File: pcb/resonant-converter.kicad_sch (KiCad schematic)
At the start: 60 parts, among them J1 Banana_Jack_Keystone_575-8, J2 Banana_Jack_Keystone_575-8, J3 Banana_Jack_Keystone_575-8, J4 Banana_Jack_Keystone_575-8, Q1 MDU04N010VRH, Q2 MDU04N010VRH, Q3 HSU30N20, Q4 HSU30N20, T1 B66206W1110T001, U1 UCC256610DDBR, U2 TEA2096T/1J, U4 PC817X2CSP9F, U5 TL431AIDBVR

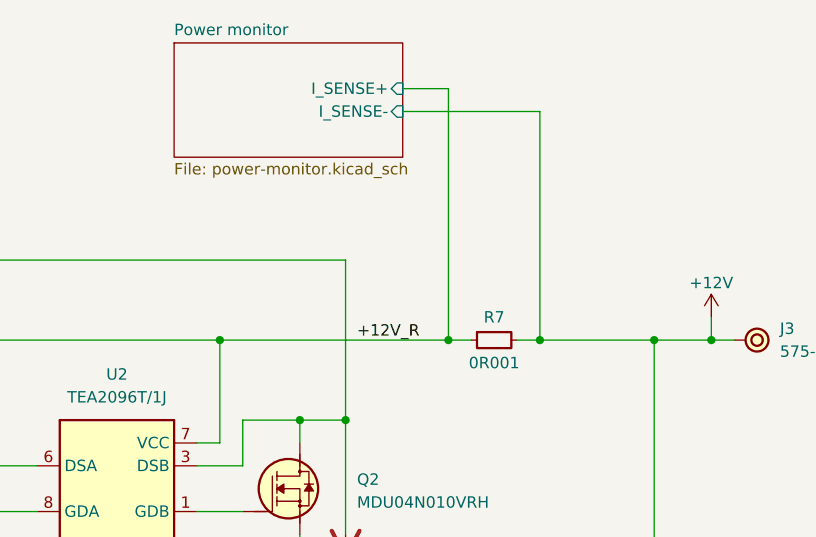
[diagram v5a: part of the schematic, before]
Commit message: [#4] Sch: Add I2C pullups, write down INA219's address, add hierarchical label for power monitor's GND
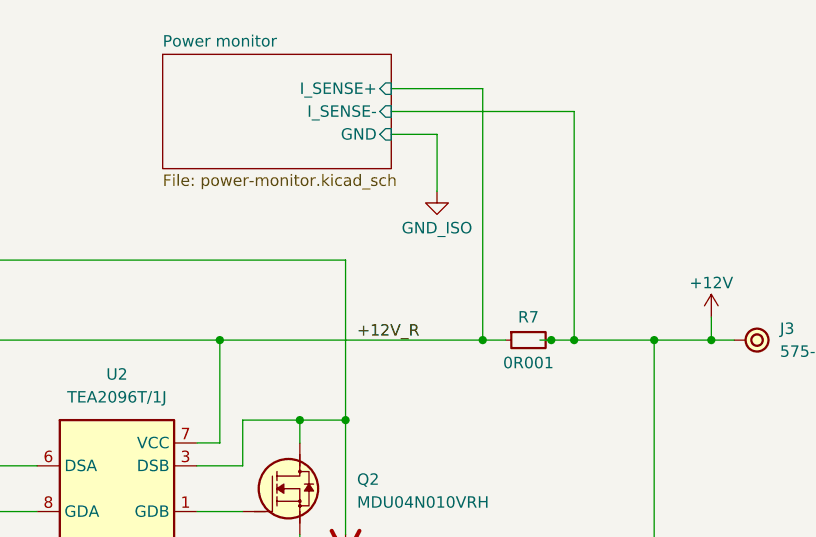
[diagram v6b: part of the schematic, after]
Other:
- sheet Power monitor ports: added GND; removed none
- moved on the sheet: R7
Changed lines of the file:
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@@
 	)
 	(junction
-		(at 361.95 107.95)
-		(diameter 0)
-		(color 0 0 0 0)
-	)
-	(junction
 		(at 369.57 147.32)
 		(diameter 0)
@@
 	)
 	(junction
-		(at 372.11 107.95)
-		(diameter 0)
-		(color 0 0 0 0)
-	)
-	(junction
 		(at 142.24 116.84)
 		(diameter 0)
@@
 	)
 	(junction
+		(at 373.38 107.95)
+		(diameter 0)
+		(color 0 0 0 0)
+	)
+	(junction
 		(at 345.44 132.08)
 		(diameter 0)
@@
 	)
 	(junction
+		(at 375.92 107.95)
+		(diameter 0)
+		(color 0 0 0 0)
+	)
+	(junction
 		(at 33.02 152.4)
 		(diameter 0)
@@
 	)
 	(junction
+		(at 365.76 107.95)
+		(diameter 0)
+		(color 0 0 0 0)
+	)
+	(junction
 		(at 306.07 147.32)
 		(diameter 0)
@@
 	(wire
 		(pts
+			(xy 365.76 107.95) (xy 368.3 107.95)
+		)
+		(stroke
+			(width 0)
+			(type default)
+		)
+	)
+	(wire
+		(pts
 			(xy 369.57 161.29) (xy 369.57 147.32)
 		)
@@
 	(wire
 		(pts
-			(xy 361.95 80.01) (xy 361.95 107.95)
+			(xy 365.76 80.01) (xy 365.76 107.95)
 		)
 		(stroke
@@
 	(wire
 		(pts
+			(xy 360.68 85.09) (xy 355.6 85.09)
+		)
+		(stroke
+			(width 0)
+			(type default)
+		)
+	)
+	(wire
+		(pts
 			(xy 304.8 116.84) (xy 311.15 116.84)
 		)
@@
 	(wire
 		(pts
-			(xy 361.95 107.95) (xy 364.49 107.95)
-		)
-		(stroke
-			(width 0)
-			(type default)
-		)
-	)
-	(wire
-		(pts
 			(xy 384.81 147.32) (xy 375.92 147.32)
 		)
@@
 	(wire
 		(pts
+			(xy 375.92 107.95) (xy 373.38 107.95)
+		)
+		(stroke
+			(width 0)
+			(type default)
+		)
+	)
+	(wire
+		(pts
 			(xy 304.8 116.84) (xy 304.8 119.38)
 		)
@@
 	(wire
 		(pts
+			(xy 373.38 107.95) (xy 372.11 107.95)
+		)
+		(stroke
+			(width 0)
+			(type default)
+		)
+	)
+	(wire
+		(pts
 			(xy 356.87 147.32) (xy 363.22 147.32)
 		)
@@
 	(wire
 		(pts
+			(xy 375.92 107.95) (xy 384.81 107.95)
+		)
+		(stroke
+			(width 0)
+			(type default)
+		)
+	)
+	(wire
+		(pts
 			(xy 39.37 147.32) (xy 39.37 152.4)
 		)
@@
 	(wire
 		(pts
-			(xy 372.11 107.95) (xy 384.81 107.95)
-		)
-		(stroke
-			(width 0)
-			(type default)
-		)
-	)
-	(wire
-		(pts
 			(xy 322.58 147.32) (xy 328.93 147.32)
 		)
@@
 	(wire
 		(pts
-			(xy 336.55 107.95) (xy 361.95 107.95)
+			(xy 336.55 107.95) (xy 365.76 107.95)
 		)
 		(stroke
@@
 	(wire
 		(pts
-			(xy 372.11 107.95) (xy 372.11 82.55)
+			(xy 375.92 107.95) (xy 375.92 82.55)
 		)
 		(stroke
@@
 	(wire
 		(pts
-			(xy 356.87 82.55) (xy 372.11 82.55)
+			(xy 355.6 82.55) (xy 375.92 82.55)
 		)
 		(stroke
@@
 	(wire
 		(pts
+			(xy 360.68 91.44) (xy 360.68 85.09)
+		)
+		(stroke
+			(width 0)
+			(type default)
+		)
+	)
+	(wire
+		(pts
 			(xy 294.64 147.32) (xy 302.26 147.32)
 		)
@@
 	(wire
 		(pts
-			(xy 356.87 80.01) (xy 361.95 80.01)
+			(xy 355.6 80.01) (xy 365.76 80.01)
 		)
 		(stroke
@@
 	(wire
 		(pts
-			(xy 369.57 107.95) (xy 372.11 107.95)
-		)
-		(stroke
-			(width 0)
-			(type default)
-		)
-	)
-	(wire
-		(pts
 			(xy 102.87 129.54) (xy 102.87 125.73)
 		)
@@
 	(symbol
 		(lib_id "DW-resistors:R-0R001-1206")
-		(at 364.49 107.95 0)
+		(at 368.3 107.95 0)
 		(unit 1)
 		(exclude_from_sim no)
@@
 		(dnp no)
 		(property "Reference" "R7"
-			(at 367.03 105.41 0)
+			(at 370.84 105.41 0)
 			(effects
 				(font
@@
 		)
 		(property "Value" "R-0R001-1206"
-			(at 377.19 110.49 0)
+			(at 381 110.49 0)
 			(effects
 				(font
@@
 		)
 		(property "Footprint" "DW-footprints:R_1206_3216Metric"
-			(at 377.19 113.03 0)
+			(at 381 113.03 0)
 			(effects
 				(font
@@
 		)
 		(property "Datasheet" "https://www.lcsc.com/datasheet/C7419993.pdf"
-			(at 377.19 115.57 0)
+			(at 381 115.57 0)
 			(effects
 				(font
@@
 		)
 		(property "Description" "1W 1mΩ ±50ppm/℃ Current Sense Resistor ±5% 1206 Current Sense Resistors RoHS"
-			(at 377.19 118.11 0)
+			(at 381 118.11 0)
 			(effects
 				(font
@@
 		)
 		(property "Manufacturer" "FOJAN"
-			(at 377.19 120.65 0)
+			(at 381 120.65 0)
 			(effects
 				(font
@@
 		)
 		(property "MPN" "FRM121WJR001TM"
-			(at 377.19 123.19 0)
+			(at 381 123.19 0)
 			(effects
 				(font
@@
 		)
 		(property "LCSC" "C7419993"
-			(at 377.19 125.73 0)
+			(at 381 125.73 0)
 			(effects
 				(font
@@
 		)
 		(property "Val" "0R001"
-			(at 367.03 110.49 0)
+			(at 370.84 110.49 0)
 			(effects
 				(font
@@
 		)
 		(property "Tolerance" "5%"
-			(at 377.19 130.81 0)
+			(at 381 130.81 0)
 			(effects
 				(font
@@
 	)
 	(symbol
+		(lib_id "DW-power-symbols:GND")
+		(at 360.68 91.44 0)
+		(unit 1)
+		(exclude_from_sim no)
+		(in_bom yes)
+		(on_board yes)
+		(dnp no)
+		(property "Reference" "#PWR019"
+			(at 360.68 97.79 0)
+			(effects
+				(font
+					(size 1.27 1.27)
+				)
+				(hide yes)
+			)
+		)
+		(property "Value" "GND_ISO"
+			(at 360.68 95.504 0)
+			(effects
+				(font
+					(size 1.27 1.27)
+				)
+			)
+		)
+		(property "Footprint" ""
+			(at 360.68 91.44 0)
+			(effects
+				(font
+					(size 1.27 1.27)
+				)
+				(hide yes)
+			)
+		)
+		(property "Datasheet" ""
+			(at 360.68 91.44 0)
+			(effects
+				(font
+					(size 1.27 1.27)
+				)
+				(hide yes)
+			)
+		)
+		(property "Description" "Power symbol creates a global label with name \"GND\" , ground"
+			(at 360.68 91.44 0)
+			(effects
+				(font
+					(size 1.27 1.27)
+				)
+				(hide yes)
+			)
+		)
+		(pin "1"
+		)
+		(instances
+			(project "resonant-converter"
+				(path "/da6185c3-cd85-4a88-bee6-2ff386eae772"
+					(reference "#PWR019")
+					(unit 1)
+				)
+			)
+		)
+	)
+	(symbol
 		(lib_id "DW-capacitors:C-10u-0603")
 		(at 322.58 166.37 90)
@@
 	)
 	(sheet
-		(at 331.47 74.93)
+		(at 330.2 76.2)
 		(size 25.4 12.7)
 		(exclude_from_sim no)
@@
 		)
 		(property "Sheetname" "Power monitor"
-			(at 331.47 74.2184 0)
+			(at 330.2 75.4884 0)
 			(effects
 				(font
@@
 		)
 		(property "Sheetfile" "power-monitor.kicad_sch"
-			(at 331.47 88.2146 0)
+			(at 330.2 89.4846 0)
 			(effects
 				(font
@@
 		)
 		(pin "I_SENSE-" input
-			(at 356.87 82.55 0)
+			(at 355.6 82.55 0)
 			(effects
 				(font
@@
 		)
 		(pin "I_SENSE+" input
-			(at 356.87 80.01 0)
+			(at 355.6 80.01 0)
+			(effects
+				(font
+					(size 1.27 1.27)
+				)
+				(justify right)
+			)
+		)
+		(pin "GND" input
+			(at 355.6 85.09 0)
 			(effects
 				(font

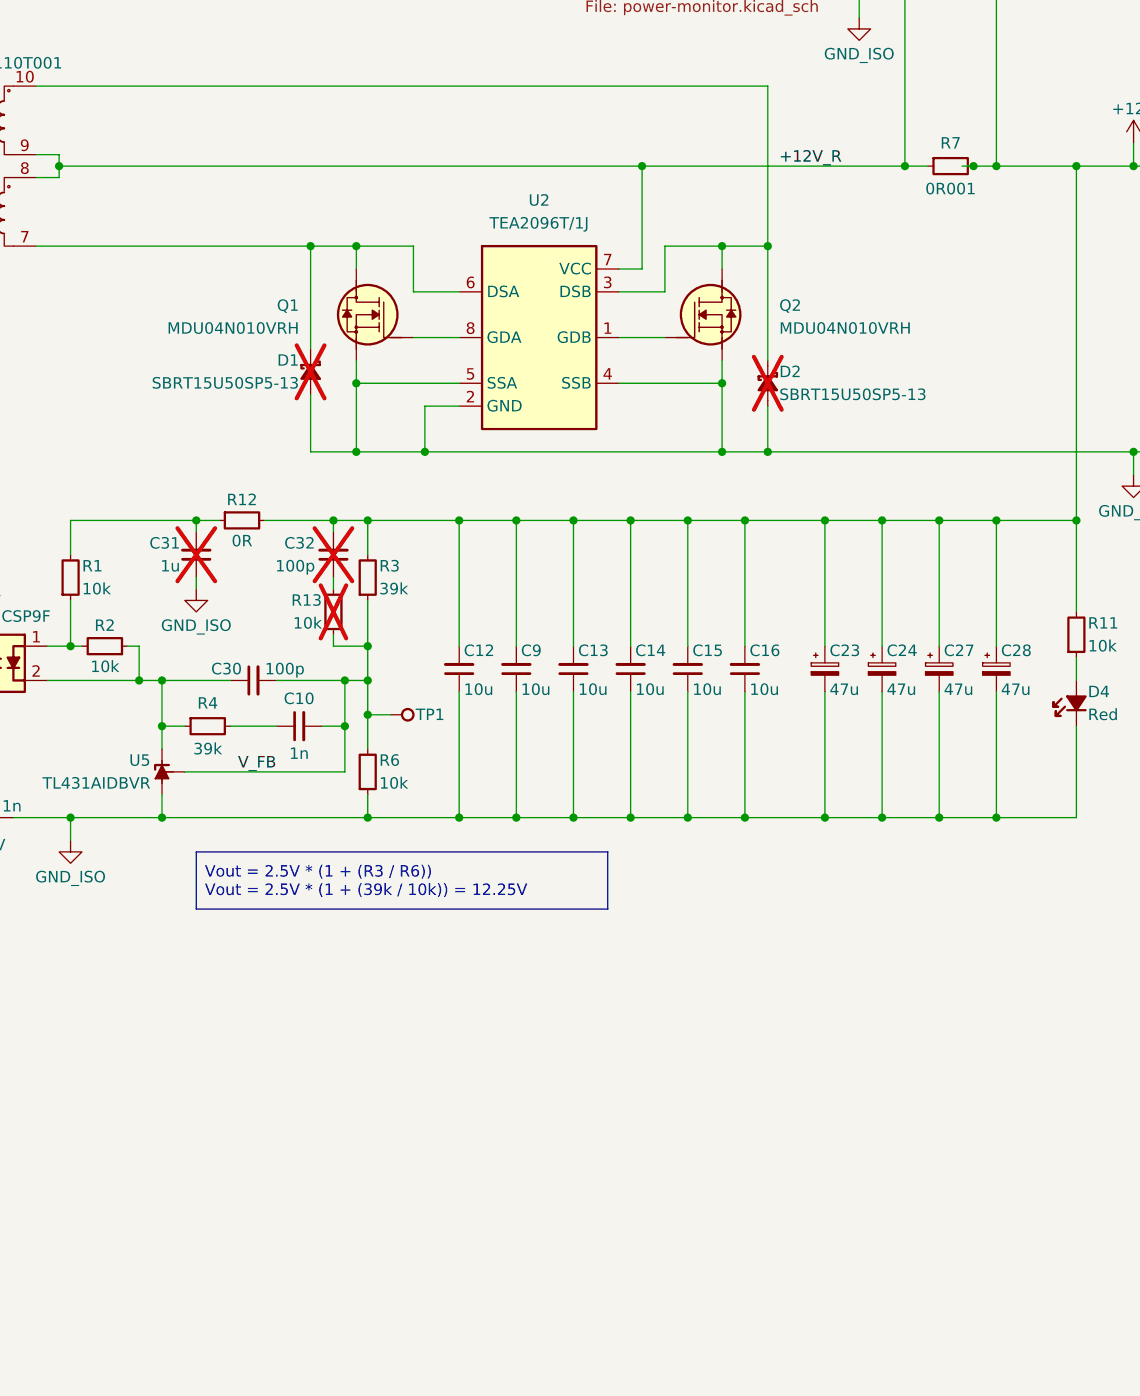
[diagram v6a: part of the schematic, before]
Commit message: [#4] Sch: Add optional fan connector
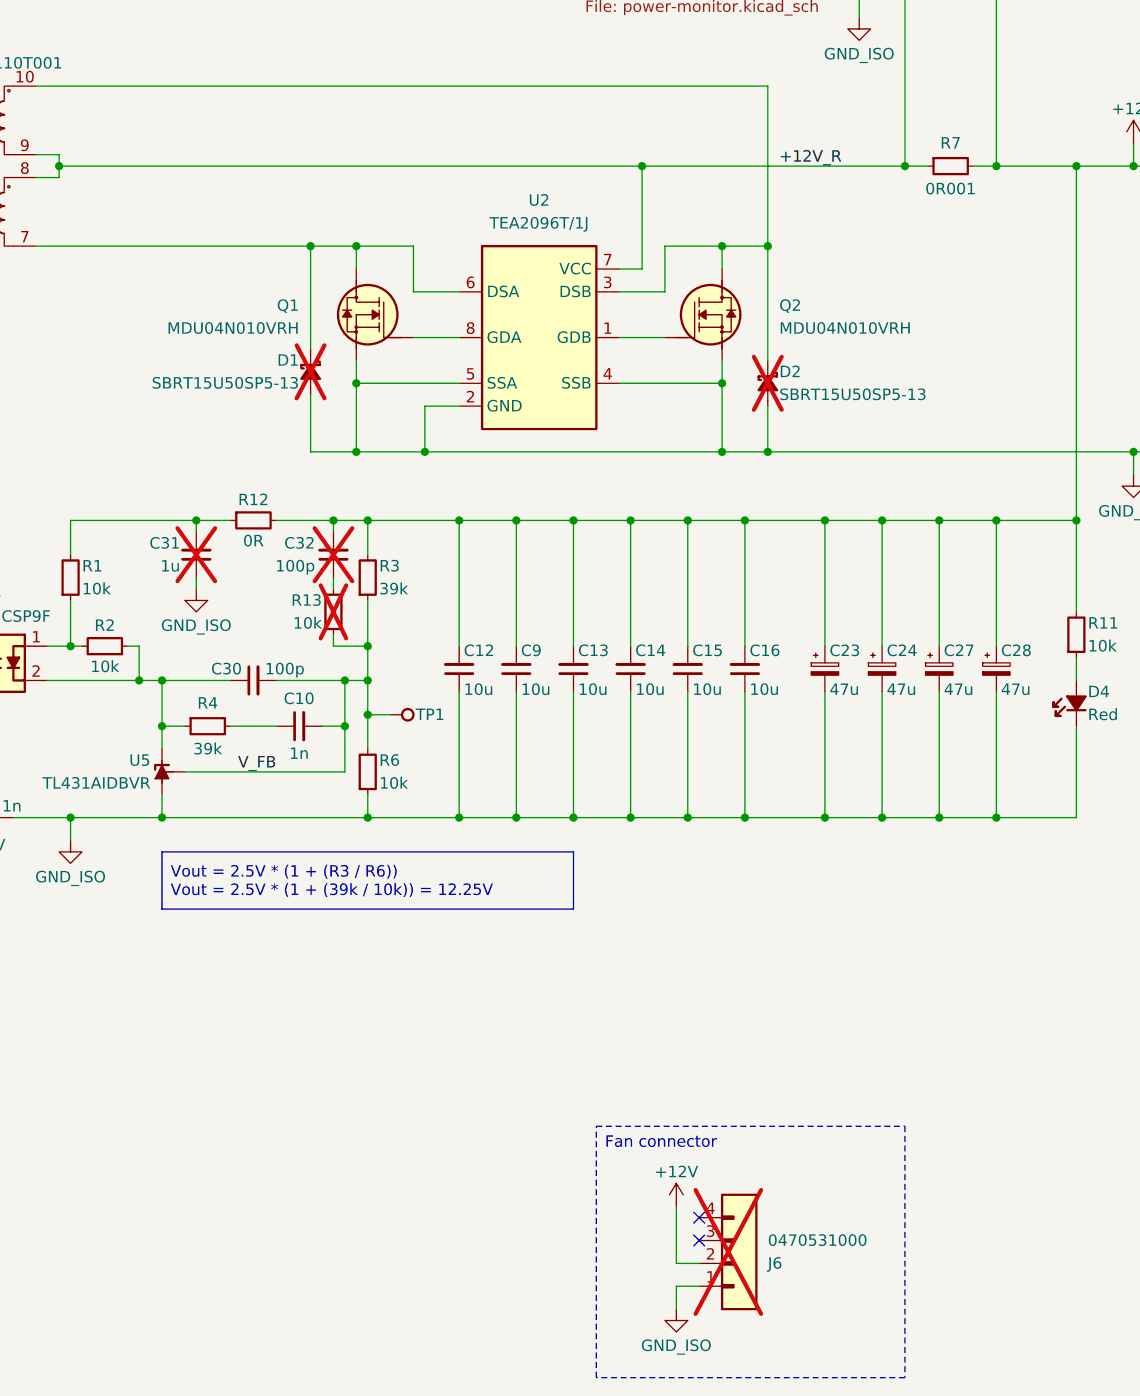
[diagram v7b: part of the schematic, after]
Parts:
- added J6: Molex_KK_1x4_0470531000, DW-footprints:Conn_Molex_KK_1x4_0470531000, symbol DW-connectors:Molex_KK_1x4_0470531000
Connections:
- net +12V: now also J6.2
- net GND_ISO: now also J6.1
- no-connect marks 0 -> 2
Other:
- moved on the sheet: R12
